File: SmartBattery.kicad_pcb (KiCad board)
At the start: 2 copper layers, 100 x 70 mm, 208 parts, among them J1 USB_C_Receptacle_USB2.0, J10 JST 2P-1.0, J11 JST 2P-1.0, J2 ST-USB-003A, J3 Barrel_Jack_MountingPin, J4 JST 2P-1.0, J5 JST 2P-1.0, J6 JST 2P-1.0, J7 JST 2P-1.0, J8 JST 2P-1.0, J9 JST 2P-1.0, Q1 AO4407A, Q10 AON7400A, Q11 AON7400A, Q12 AON7400A, Q13 AON7400A, Q2 2n7002K, Q3 AON7400A, Q4 AON7400A, Q5 AON7400A, Q6 AON7400A, Q7 2n7002K, Q8 AON7400A, Q9 AON7400A, SW1 SW_Push, SW2 SW_Push, U1 bq2477x, U10 ESP32-WROOM-32U, U2 BQ294706DSGR, U3 ITV4030, U4 BQ40Z50, U5 LM5175PWPR, U6 STM32F730R8T6, U7 W25Q128JVSIQ, U8 TPS54202HDDCR, U9 FS35ND01G-S1Y2QWFI000, Y1 Q13FC1350000400, Y2 Crystal_GND24

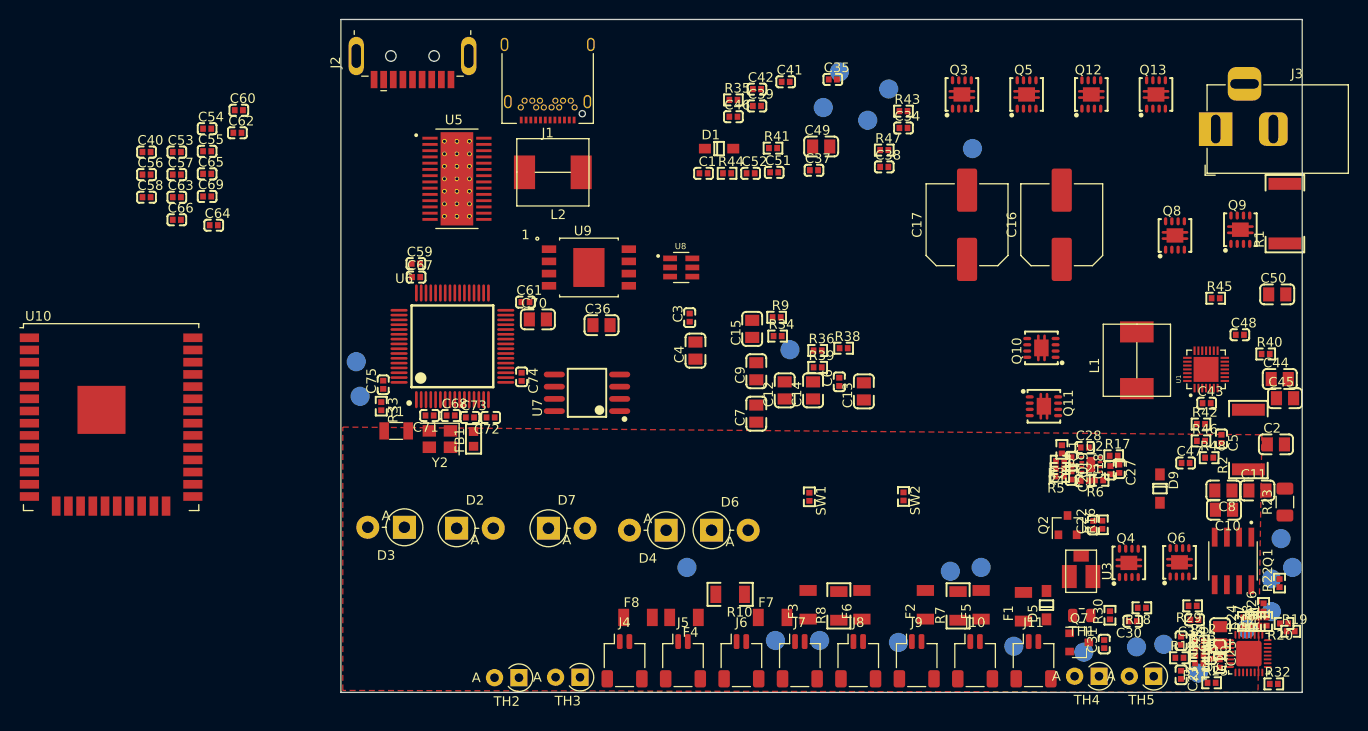
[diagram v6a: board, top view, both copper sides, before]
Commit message: Replaced old charger to support JLC assembly. Very close now!
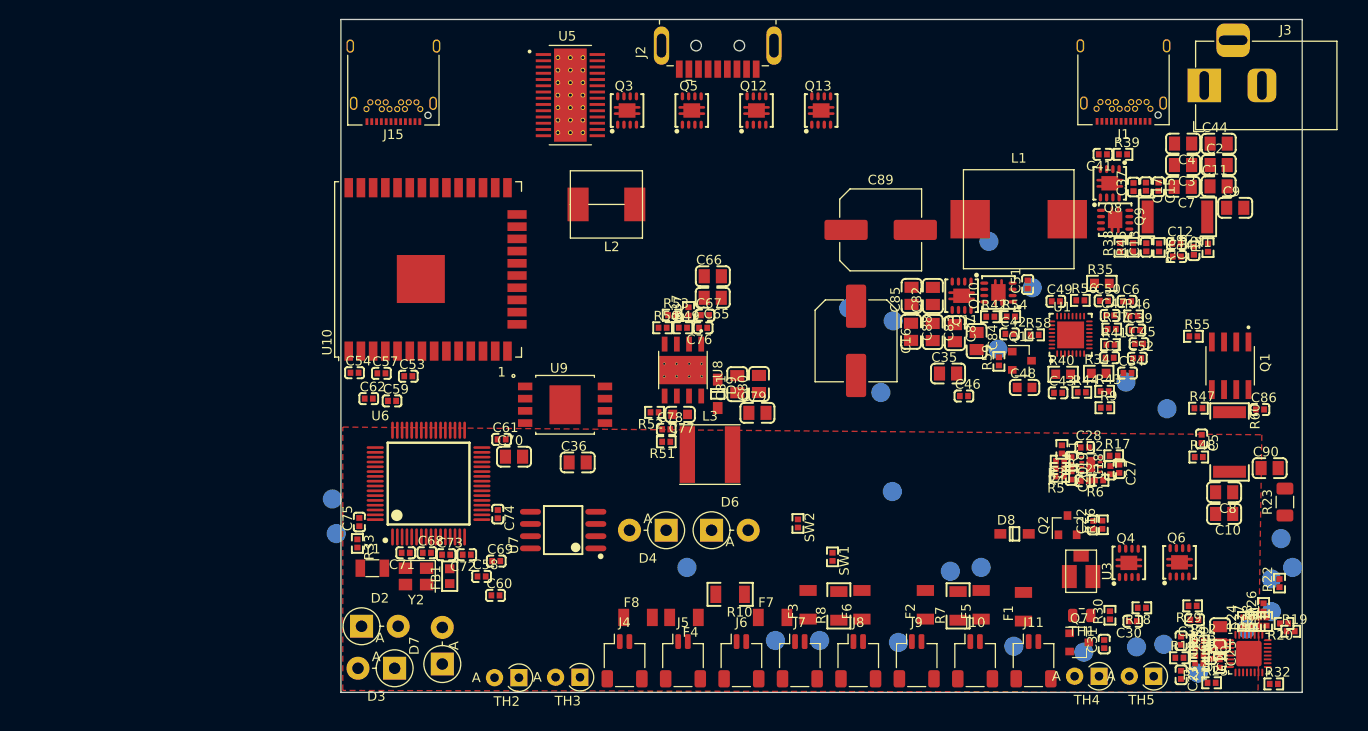
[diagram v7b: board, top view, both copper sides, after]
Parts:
- removed C40, C55, C56, C63, C64: 0.1u 6.3v, lc_lib:0402_C
- removed D1: CD1206-S01575, lc_lib:SOD-123
- removed D5: DIODE, lc_lib:SOD-123
- added C76: 0.1u 25v, lc_lib:0402_C, F.Cu at (37.7, 32.1)
- added C77: 8.2nF, lc_lib:0603_C, F.Cu at (35.3, 41.1)
- added C78: 220pF, lc_lib:0402_C, F.Cu at (33.8, 42.6)
- added C79: 22u, lc_lib:0805_C, F.Cu at (43.3, 40.9)
- added C80: 22u, lc_lib:0805_C, F.Cu at (43.5, 37.9)
- added C81: 22u, lc_lib:0805_C, F.Cu at (41.2, 37.9)
- added C82: 10u, lc_lib:0805_C, F.Cu at (61.6, 28.8)
- added C83: 10u, lc_lib:0805_C, F.Cu at (61.6, 32.5)
- added C84: 10u, lc_lib:0805_C, F.Cu at (66.1, 33.5)
- added C85: 10u, lc_lib:0805_C, F.Cu at (59.4, 28.8)
- added C86: 1uF 25v, lc_lib:0402_C, F.Cu at (95.6, 40.6)
- added C87: 22u, lc_lib:0805_C, F.Cu at (63.9, 32.6)
- added C88: 22u, lc_lib:0805_C, F.Cu at (59.3, 32.5)
- added C89: 220u, Capacitor_SMD:C_Elec_8x10.2, F.Cu at (56.1, 21.9)
- added C90: 22u, lc_lib:0805_C, F.Cu at (96.6, 46.7)
- added D8: B5817W-5819W, lc_lib:SOD-123, F.Cu at (70.1, 53.5)
- added J15: USB_C_Receptacle_USB2.0, Connector_USB:USB_C_Receptacle_Amphenol_12401548E4-2A, F.Cu at (5.46, 5.61)
- added L3: 6.8uH 47mO SWPA6028S6R8MT, Inductor_SMD:L_Taiyo-Yuden_NR-60xx, F.Cu at (38.4, 45.3)
- added Q14: 2n7002K, Package_TO_SOT_SMD:SOT-23, F.Cu at (70.8, 35.5)
- added R37: 0, lc_lib:0402_R, F.Cu at (36.2, 30.4)
- added R49: 0, lc_lib:0402_R, F.Cu at (35.6, 32.1)
- added R50: 20k, lc_lib:0402_R, F.Cu at (33.5, 32.1)
- added R51: 51k, lc_lib:0402_R, F.Cu at (33.8, 43.9)
- added R52: 15k, lc_lib:0402_R, F.Cu at (32.6, 40.9)
- added R53: DNP, lc_lib:0402_R, F.Cu at (34.5, 30.8)
- added R54: 0, lc_lib:0402_R, F.Cu at (69.7, 30.9)
- added R55: 0, lc_lib:0402_R, F.Cu at (88.7, 33.0)
- added R56: 110k, lc_lib:0402_R, F.Cu at (76.9, 29.2)
- added R57: DNP, lc_lib:0402_R, F.Cu at (80.2, 32.2)
- added R58: DNP, lc_lib:0402_R, F.Cu at (72.2, 32.8)
- added R59: 110k, lc_lib:0402_R, F.Cu at (68.5, 35.6)
- added R60: 0.01, lc_lib:2512_R, F.Cu at (92.4, 44.0)
- added TP25: TestPoint, TestPoint:TestPoint_Pad_D2.0mm, B.Cu at (71.9, 27.9)
- added TP26: TestPoint, TestPoint:TestPoint_Pad_D2.0mm, B.Cu at (67.4, 23.1)
- added TP27: TestPoint, TestPoint:TestPoint_Pad_D2.0mm, B.Cu at (85.9, 40.5)
- C1: value 1uF -> 0.1uF 6.3v
- C12: value 22u -> DNP; footprint lc_lib:0805_C -> lc_lib:0402_C
- C13: value 22u -> 1uF 25v; footprint lc_lib:0805_C -> lc_lib:0402_C
- C14, C15: value 22u -> 33nF; footprint lc_lib:0805_C -> lc_lib:0402_C
- C17: value 220u -> 33nF; footprint Capacitor_SMD:C_Elec_8x10.2 -> lc_lib:0402_C
- C3: value 0.1u 25v -> 10u; footprint lc_lib:0402_C -> lc_lib:0805_C
- C34: value 1uF 16v -> 0.1uF 6.3v
- C35: value 1uF 16v -> 2.2u 50v; footprint lc_lib:0402_C -> lc_lib:0805_C
- C37: value 1uF 25v -> 150pF
- C38: value 0.1uF 25v -> 33nF
- C39: value 0.1uF -> 33pF
- C4, C7, C9: value 22u -> 10u
- C41: value 0.1uF 25v -> 150pF
- C42: value 0.01uF -> 150pF
- C43: value 1uF 25v -> 0.1uF 25v
- C45: value 2.2uF 25v -> 150pF; footprint lc_lib:0805_C -> lc_lib:0402_C
- C46: value 2200pF -> 0.1uF 25v
- C47: value 0.1uF -> 1.5nF
- C48: value 1uF 25v -> 680pF; footprint lc_lib:0402_C -> lc_lib:0603_C
- C49: value 10u -> 15pF; footprint lc_lib:0805_C -> lc_lib:0402_C
- C50: value 10u -> 1uF 16v; footprint lc_lib:0805_C -> lc_lib:0402_C
- C51: value 47n -> 150pF
- C52: value 0.1uF 25v -> 1uF 16v
- C6: value 0.1u 25v -> 0.1uF 6.3v
- C65, C66: value 0.1u 6.3v -> 10u; footprint lc_lib:0402_C -> lc_lib:0805_C
- C67: value 0.1u 6.3v -> 0.1u 25v
- D9: value CD1206-S01575 -> B5817W-5819W
- L1: value MWSA0603-2R2MT -> MWSA1004-2R2MT; footprint SmartBattery:MWSA0603 -> SmartBattery:L_10.3x11.5_H4
- R2: value 0.01 -> 4.7; footprint lc_lib:2512_R -> lc_lib:0402_R
- R34: value 10M -> 27k; footprint lc_lib:0402_R -> lc_lib:0603_R
- R35: value DNP -> 110k; footprint lc_lib:0402_R -> lc_lib:0603_R
- R36: value 0 -> 4.7
- R39: value 1M -> 0
- R40: value 430k -> 40.2k; footprint lc_lib:0402_R -> lc_lib:0603_R
- R41: value 100k -> 10k
- R42: value 4.7 -> 0
- R43, R44: value 4.02k -> 0
- R45: value 10 -> 1
- R46, R47: value 0 -> 10
- R48: value 4.7 -> 10
- R9: value 10M -> 33k
- U1: value bq2477x -> BQ25703ARSNR; footprint SmartBattery:QFN40P400X400X80-29N -> lc_lib:VQFN-32_4X4X04P
- U8: value TPS54202HDDCR -> LMR14030SDDAR; footprint SmartBattery:SOT95P280X110-6N -> SmartBattery:NOPB
- moved J1 59.9 mm to (81.4, 5.58)
- moved C60 57.1 mm to (16.1, 59.9)
- moved C66 56.1 mm to (38.7, 26.7)
- moved C4 55.1 mm to (87.6, 12.9), turned to 180 degrees
- moved C65 54.2 mm to (38.7, 28.9), turned to 180 degrees
- moved C3 53.7 mm to (87.6, 15.1), turned to 180 degrees
- moved C58 52.6 mm to (14.6, 57.9)
- moved C9 52.6 mm to (93.0, 19.6), turned to 0 degrees
- moved C7 50.2 mm to (87.6, 17.4), turned to 180 degrees
- moved C69 48.4 mm to (16.2, 56.3)
- moved D9 47.0 mm to (39.2, 38.9)
- moved C1 46.4 mm to (80.0, 35.2)
- moved C39 45.8 mm to (82.7, 32.3)
- moved C15 44.8 mm to (85.0, 17.4), turned to 270 degrees
- moved C52 44.6 mm to (82.8, 35.2)
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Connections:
- net /Charger/ACOK renamed /Charger/EN_OTG
- net Net-(J2-Pad1) renamed /OutputStage/OUTPUT_VOLTAGE
- C10 pad 1: Net-(C10-Pad1) -> /Battery connection and protection/BATT_PACK_P
- C11 pad 1: Net-(C10-Pad1) -> /Charger/ADAPTER_IN
- C12 pad 1: /Charger/VSYS -> Net-(C12-Pad1)
- C12 pad 2: GND -> Net-(C12-Pad2)
- C13 pad 1: /Charger/VSYS -> GND
- C13 pad 2: GND -> Net-(C13-Pad2)
- C14 pad 1: /Charger/VSYS -> Net-(C12-Pad1)
- C15 pad 1: /Charger/VSYS -> GND
- C15 pad 2: GND -> Net-(C15-Pad2)
- C17 pad 1: /Charger/VSYS -> GND
- C17 pad 2: GND -> Net-(C15-Pad2)
- C2 pad 1: /Charger/VSYS -> /Charger/ADAPTER_IN
- C3 pad 1: /Charger/VSYS -> /Charger/ADAPTER_IN
- C36 pad 2: /MCU/Power_3p3v -> /Peripheral_3p3v/3p3v
- C37 pad 1: GND -> Net-(C15-Pad2)
- C37 pad 2: Net-(C37-Pad2) -> GND
- C38 pad 1: Net-(C37-Pad2) -> GND
- C38 pad 2: GND -> Net-(C12-Pad2)
- C39 pad 1: Net-(C37-Pad2) -> GND
- C4 pad 1: /Charger/VSYS -> /Charger/ADAPTER_IN
- C41 pad 1: Net-(C39-Pad2) -> GND
- C41 pad 2: GND -> Net-(C41-Pad2)
- C43 pad 1: GND -> Net-(C43-Pad1)
- C43 pad 2: /Charger/BQ_VCC -> Net-(C43-Pad2)
- C45 pad 1: /Charger/ADAPTER_IN -> GND
- C45 pad 2: GND -> Net-(C42-Pad2)
- C46 pad 2: /Charger/ADAPTER_IN -> Net-(C46-Pad2)
- C47 pad 1: Net-(C47-Pad1) -> GND
- C47 pad 2: Net-(C46-Pad1) -> Net-(C42-Pad2)
- C48 pad 1: GND -> Net-(C48-Pad1)
- C48 pad 2: Net-(C39-Pad2) -> GND
- C49 pad 1: Net-(C39-Pad2) -> Net-(C49-Pad1)
- C5 pad 1: /Charger/VSYS -> Net-(C5-Pad1)
- C5 pad 2: Net-(C10-Pad1) -> /Battery connection and protection/BATT_PACK_P
- C50 pad 1: Net-(C39-Pad2) -> Net-(C50-Pad1)
- C51 pad 1: Net-(C51-Pad1) -> GND
- C52 pad 1: /Battery connection and protection/BATT_PACK_P -> Net-(C52-Pad1)
- C53 pad 1: /MCU/Power_3p3v -> /Peripheral_3p3v/3p3v
- C54 pad 1: /MCU/Power_3p3v -> /Peripheral_3p3v/3p3v
- C57 pad 1: /MCU/Power_3p3v -> /Peripheral_3p3v/3p3v
- C59 pad 1: /MCU/Power_3p3v -> /Peripheral_3p3v/3p3v
- C6 pad 1: Net-(C10-Pad1) -> GND
- C6 pad 2: GND -> /Charger/PSYS
- C61 pad 1: /MCU/Power_3p3v -> /Peripheral_3p3v/3p3v
- C62 pad 1: /MCU/Power_3p3v -> /Peripheral_3p3v/3p3v
- C65 pad 1: /MCU/Power_3p3v -> GND
- C65 pad 2: GND -> /Peripheral_3p3v/VSYS_IN_3p3
- C66 pad 1: /MCU/Power_3p3v -> /Peripheral_3p3v/VSYS_IN_3p3
- C67 pad 1: /MCU/Power_3p3v -> /Peripheral_3p3v/VSYS_IN_3p3
- C7 pad 1: /Charger/VSYS -> /Charger/ADAPTER_IN
- C74 pad 1: /MCU/Power_3p3v -> /Peripheral_3p3v/3p3v
- C75 pad 1: /MCU/Power_3p3v -> /Peripheral_3p3v/3p3v
- C8 pad 1: Net-(C10-Pad1) -> /Battery connection and protection/BATT_PACK_P
- C9 pad 1: /Charger/VSYS -> /Charger/ADAPTER_IN
- D9 pad 1: /Charger/BQ_VCC -> Net-(D9-Pad1)
- D9 pad 2: /Battery connection and protection/BATT_PACK_P -> GND
- FB1 pad 1: /MCU/Power_3p3v -> /Peripheral_3p3v/3p3v
- J2 pad 4: Net-(J2-Pad4) -> GND
- J2 pad 5: Net-(J2-Pad5) -> GND
- J3 pad 1: Net-(J3-Pad1) -> /Charger/ADAPTER_IN
- J3 pad 2: Net-(J3-Pad2) -> GND
- L1 pad 1: /Charger/VSYS -> Net-(C46-Pad1)
- L1 pad 2: Net-(C51-Pad1) -> Net-(C43-Pad1)
- Q1 pad 1: Net-(C10-Pad1) -> /Charger/VSYS
- Q1 pad 2: Net-(C10-Pad1) -> /Charger/VSYS
- Q1 pad 3: Net-(C10-Pad1) -> /Charger/VSYS
- Q1 pad 5: /Battery connection and protection/BATT_PACK_P -> Net-(C5-Pad1)
- Q1 pad 6: /Battery connection and protection/BATT_PACK_P -> Net-(C5-Pad1)
- Q1 pad 7: /Battery connection and protection/BATT_PACK_P -> Net-(C5-Pad1)
- Q1 pad 8: /Battery connection and protection/BATT_PACK_P -> Net-(C5-Pad1)
- Q10 pad 1: Net-(C51-Pad1) -> GND
- Q10 pad 2: Net-(C51-Pad1) -> GND
- Q10 pad 3: Net-(C51-Pad1) -> GND
- Q10 pad 4: Net-(Q10-Pad4) -> Net-(C51-Pad2)
- Q10 pad 5: Net-(C39-Pad2) -> Net-(C46-Pad1)
- Q10 pad 6: Net-(C39-Pad2) -> Net-(C46-Pad1)
- Q10 pad 7: Net-(C39-Pad2) -> Net-(C46-Pad1)
- Q10 pad 8: Net-(C39-Pad2) -> Net-(C46-Pad1)
- Q11 pad 1: GND -> Net-(C46-Pad1)
- Q11 pad 2: GND -> Net-(C46-Pad1)
- Q11 pad 3: GND -> Net-(C46-Pad1)
- Q11 pad 5: Net-(C51-Pad1) -> /Charger/VSYS
- Q11 pad 6: Net-(C51-Pad1) -> /Charger/VSYS
- Q11 pad 7: Net-(C51-Pad1) -> /Charger/VSYS
- Q11 pad 8: Net-(C51-Pad1) -> /Charger/VSYS
- Q8 pad 1: Net-(C47-Pad1) -> GND
- Q8 pad 2: Net-(C47-Pad1) -> GND
- Q8 pad 3: Net-(C47-Pad1) -> GND
- Q8 pad 4: Net-(Q8-Pad4) -> Net-(C41-Pad2)
- Q8 pad 5: /Charger/ADAPTER_IN -> Net-(C43-Pad1)
- Q8 pad 6: /Charger/ADAPTER_IN -> Net-(C43-Pad1)
- Q8 pad 7: /Charger/ADAPTER_IN -> Net-(C43-Pad1)
- Q8 pad 8: /Charger/ADAPTER_IN -> Net-(C43-Pad1)
- Q9 pad 1: Net-(C47-Pad1) -> Net-(C43-Pad1)
- Q9 pad 2: Net-(C47-Pad1) -> Net-(C43-Pad1)
- Q9 pad 3: Net-(C47-Pad1) -> Net-(C43-Pad1)
- Q9 pad 4: Net-(Q8-Pad4) -> Net-(Q9-Pad4)
- Q9 pad 5: Net-(C37-Pad2) -> Net-(C15-Pad2)
- Q9 pad 6: Net-(C37-Pad2) -> Net-(C15-Pad2)
- Q9 pad 7: Net-(C37-Pad2) -> Net-(C15-Pad2)
- Q9 pad 8: Net-(C37-Pad2) -> Net-(C15-Pad2)
- R1 pad 1: Net-(C39-Pad2) -> /Charger/ADAPTER_IN
- R1 pad 2: Net-(C37-Pad2) -> Net-(C15-Pad2)
- R2 pad 1: Net-(C10-Pad1) -> Net-(C15-Pad2)
- R2 pad 2: /Charger/VSYS -> Net-(C12-Pad1)
- R33 pad 1: /MCU/Power_3p3v -> /Peripheral_3p3v/3p3v
- R34 pad 1: /Charger/REGN -> GND
- R35 pad 1: Net-(C42-Pad2) -> /Charger/IADP
- R35 pad 2: /Charger/REGN -> Net-(R34-Pad2)
- R36 pad 1: Net-(R36-Pad1) -> /Charger/ADAPTER_IN
- R36 pad 2: Net-(C37-Pad2) -> Net-(C12-Pad2)
- R38 pad 1: Net-(R38-Pad1) -> Net-(Q9-Pad4)
- R38 pad 2: Net-(C39-Pad2) -> Net-(R38-Pad2)
- R39 pad 1: Net-(C42-Pad2) -> Net-(R39-Pad1)
- R39 pad 2: GND -> Net-(C41-Pad2)
- R40 pad 1: Net-(R40-Pad1) -> Net-(C39-Pad2)
- R40 pad 2: /Charger/ADAPTER_IN -> Net-(C42-Pad2)
- R41 pad 1: GND -> Net-(C49-Pad1)
- R41 pad 2: Net-(R40-Pad1) -> Net-(C48-Pad1)
- R42 pad 1: Net-(Q8-Pad4) -> Net-(R42-Pad1)
- R42 pad 2: Net-(C46-Pad1) -> Net-(C51-Pad2)
- R43 pad 1: Net-(C47-Pad1) -> Net-(R43-Pad1)
- R44 pad 1: Net-(C46-Pad1) -> Net-(R44-Pad1)
- R45 pad 1: Net-(R45-Pad1) -> Net-(C13-Pad2)
- R45 pad 2: /Charger/BQ_VCC -> Net-(C15-Pad2)
- R46 pad 1: Net-(R46-Pad1) -> /Charger/REGN
- R46 pad 2: Net-(Q10-Pad4) -> Net-(C50-Pad1)
- R47 pad 2: Net-(Q11-Pad4) -> Net-(C5-Pad1)
- R48 pad 1: /Battery connection and protection/BATT_PACK_P -> Net-(R48-Pad1)
- R48 pad 2: Net-(R48-Pad2) -> /Battery connection and protection/BATT_PACK_P
- R9 pad 2: /Charger/PMON -> /Charger/PSYS
- TP20 pad 1: Net-(C47-Pad1) -> Net-(C43-Pad1)
- TP21 pad 1: Net-(C37-Pad2) -> Net-(C12-Pad1)
- TP22 pad 1: Net-(C39-Pad2) -> Net-(C12-Pad2)
- U1 pad 1: Net-(R38-Pad1) -> Net-(C13-Pad2)
- U1 pad 10: /Charger/PROCHOT_N -> /Charger/PSYS
- U1 pad 11: /Charger/CHARGER_SDA -> /Charger/PROCHOT_N
- U1 pad 12: /Charger/CHARGER_SCL -> /Charger/CHARGER_SDA
- U1 pad 13: Net-(U1-Pad13) -> /Charger/CHARGER_SCL
- U1 pad 14: Net-(U1-Pad14) -> Net-(R43-Pad2)
- U1 pad 15: Net-(U1-Pad15) -> Net-(R44-Pad1)
- U1 pad 16: Net-(R34-Pad2) -> Net-(C39-Pad2)
- U1 pad 17: Net-(R48-Pad2) -> Net-(C49-Pad1)
- U1 pad 18: Net-(Q1-Pad4) -> Net-(Q14-Pad2)
- U1 pad 19: /Charger/VSYS -> Net-(R48-Pad1)
- U1 pad 2: Net-(R36-Pad1) -> Net-(C12-Pad1)
- U1 pad 20: Net-(C10-Pad1) -> Net-(R47-Pad1)
- U1 pad 21: Net-(C42-Pad2) -> Net-(R55-Pad1)
- U1 pad 22: GND -> /Charger/VSYS
- U1 pad 23: Net-(R47-Pad1) -> Net-(C46-Pad1)
- U1 pad 24: /Charger/REGN -> Net-(R54-Pad1)
- U1 pad 25: (no net) -> Net-(C46-Pad2)
- U1 pad 26: Net-(R46-Pad1) -> Net-(R42-Pad1)
- U1 pad 27: Net-(C51-Pad1) -> GND
- U1 pad 28: Net-(R45-Pad1) -> /Charger/REGN
- U1 pad 29: GND -> Net-(R39-Pad1)
- U1 pad 3: Net-(R43-Pad2) -> Net-(C12-Pad2)
- U1 pad 4: Net-(R44-Pad2) -> /Charger/CHRG_OK
- U1 pad 6: Net-(R40-Pad1) -> Net-(C52-Pad1)
- U1 pad 7: /Charger/IADP -> Net-(C50-Pad1)
- U1 pad 8: /Charger/IBAT -> /Charger/IADP
- U1 pad 9: /Charger/PMON -> /Charger/IBAT
- U6 pad 19: /MCU/Power_3p3v -> /Peripheral_3p3v/3p3v
- U6 pad 32: /MCU/Power_3p3v -> /Peripheral_3p3v/3p3v
- U6 pad 48: /MCU/Power_3p3v -> /Peripheral_3p3v/3p3v
- U6 pad 64: /MCU/Power_3p3v -> /Peripheral_3p3v/3p3v
- U7 pad 8: /MCU/Power_3p3v -> /Peripheral_3p3v/3p3v
- U8 pad 2: Net-(U8-Pad2) -> /Peripheral_3p3v/VSYS_IN_3p3
- U9 pad 8: /MCU/Power_3p3v -> /Peripheral_3p3v/3p3v
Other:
- copper layers 2 -> 4
- net class Default: clearance 0.18 -> 0.13; trace_width 0.18 -> 0.13; via_dia 0.4 -> 0.45; via_drill 0.3 -> 0.25
- rule trace_clearance: 0.18 -> 0.13
- rule trace_min: 0.16 -> 0.12
- rule via_min_drill: 0.3 -> 0.25
- rule via_min_size: 0.4 -> 0.45

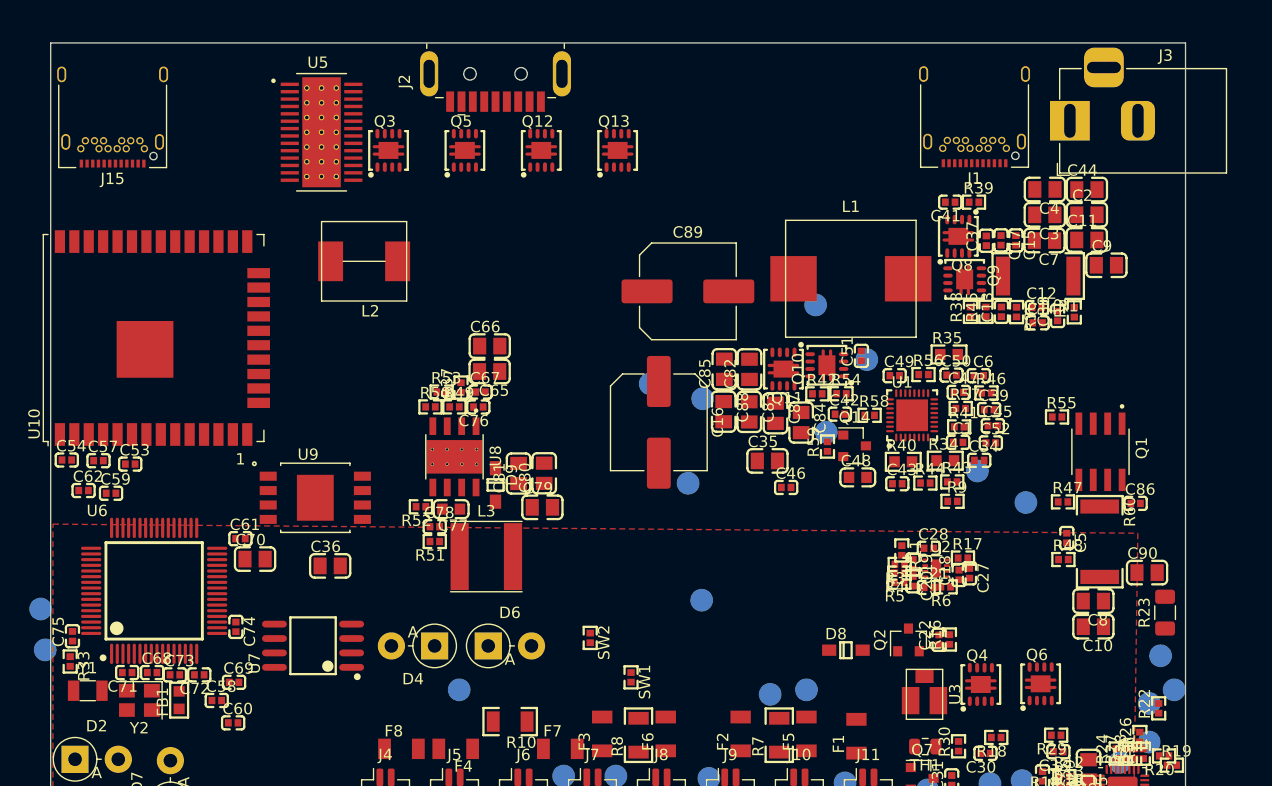
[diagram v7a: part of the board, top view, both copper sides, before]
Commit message: Both type-c ports are done! Only outputstage left.
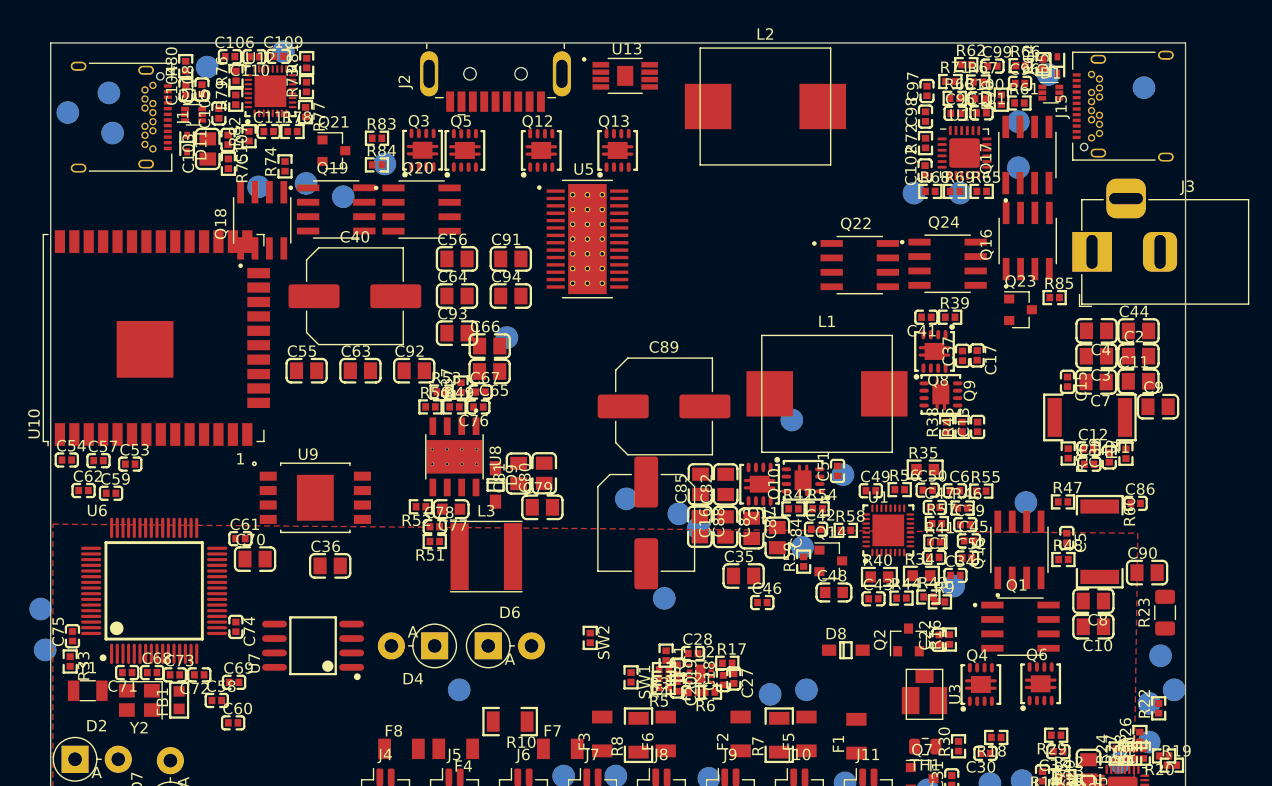
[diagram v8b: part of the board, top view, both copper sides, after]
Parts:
- added C100: 1uF 25v, lc_lib:0402_C, F.Cu at (81.9, 4.92)
- added C101: 1uF 25v, lc_lib:0402_C, F.Cu at (82.0, 6.16)
- added C102: 1uF 25v, lc_lib:0402_C, F.Cu at (77.0, 11.2)
- added C103: 10u, lc_lib:0805_C, F.Cu at (13.8, 9.34)
- added C104: 150pF, lc_lib:0402_C, F.Cu at (11.9, 4.16)
- added C105: 150pF, lc_lib:0402_C, F.Cu at (14.8, 6.21)
- added C106: 1uF 25v, lc_lib:0402_C, F.Cu at (15.8, 1.21)
- added C107: 1uF 25v, lc_lib:0402_C, F.Cu at (15.6, 8.54)
- added C108: 1uF 25v, lc_lib:0402_C, F.Cu at (13.3, 4.11)
- added C109: 1uF 25v, lc_lib:0402_C, F.Cu at (20.1, 1.18)
- added C110: 1uF 25v, lc_lib:0402_C, F.Cu at (17.9, 1.22)
- added C111: 1uF 25v, lc_lib:0402_C, F.Cu at (19.2, 7.80)
- added C40: 220u, Capacitor_SMD:C_Elec_8x10.2, F.Cu at (26.8, 22.3)
- added C55: 22u, lc_lib:0805_C, F.Cu at (22.6, 28.9)
- added C56: 22u, lc_lib:0805_C, F.Cu at (35.8, 19.0)
- added C63: 22u, lc_lib:0805_C, F.Cu at (27.3, 28.9)
- added C64: 22u, lc_lib:0805_C, F.Cu at (35.8, 22.3)
- added C91: 22u, lc_lib:0805_C, F.Cu at (40.5, 19.0)
- added C92: 22u, lc_lib:0805_C, F.Cu at (32.0, 28.9)
- added C93: 22u, lc_lib:0805_C, F.Cu at (35.8, 25.6)
- added C94: 22u, lc_lib:0805_C, F.Cu at (40.5, 22.3)
- added C95: 150pF, lc_lib:0402_C, F.Cu at (79.7, 6.20)
- added C96: 150pF, lc_lib:0402_C, F.Cu at (85.4, 3.56)
- added C97: 1uF 25v, lc_lib:0402_C, F.Cu at (77.2, 4.24)
- added C98: 1uF 25v, lc_lib:0402_C, F.Cu at (77.1, 6.49)
- added C99: 1uF 25v, lc_lib:0402_C, F.Cu at (83.0, 2.04)
- added D1: ESDA6V8AV6, Package_TO_SOT_SMD:SOT-563, F.Cu at (88.1, 4.38)
- added D10: ESDA6V8AV6, Package_TO_SOT_SMD:SOT-563, F.Cu at (12.6, 6.33)
- added D11: PESD24VS1UB-N, lc_lib:SOD-523, F.Cu at (12.0, 8.87)
- added D5: PESD24VS1UB-N, lc_lib:SOD-523, F.Cu at (88.7, 1.95)
- added Q15: VBA2625, SmartBattery:SOIC127P600X175-8N, F.Cu at (85.4, 44.7)
- added Q16: VBA2625, SmartBattery:SOIC127P600X175-8N, F.Cu at (86.1, 17.5)
- added Q17: VBA2625, SmartBattery:SOIC127P600X175-8N, F.Cu at (86.1, 9.88)
- added Q18: VBA2625, SmartBattery:SOIC127P600X175-8N, F.Cu at (18.6, 15.6)
- added Q19: VBA2625, SmartBattery:SOIC127P600X175-8N, F.Cu at (25.2, 14.7)
- added Q20: VBA2625, SmartBattery:SOIC127P600X175-8N, F.Cu at (32.7, 14.7)
- added Q21: 2n7002K, Package_TO_SOT_SMD:SOT-23, F.Cu at (25.0, 9.50)
- added Q22: VBA2625, SmartBattery:SOIC127P600X175-8N, F.Cu at (71.3, 19.6)
- added Q23: 2n7002K, Package_TO_SOT_SMD:SOT-23, F.Cu at (85.5, 23.5)
- added Q24: VBA2625, SmartBattery:SOIC127P600X175-8N, F.Cu at (79.0, 19.5)
- added R61: ??, lc_lib:0402_R, F.Cu at (85.4, 5.29)
- added R62: 100k, lc_lib:0402_R, F.Cu at (80.7, 1.91)
- added R63: 100k, lc_lib:0402_R, F.Cu at (79.7, 4.88)
- added R64: 0, lc_lib:0402_R, F.Cu at (87.4, 1.87)
- added R65: 100k, lc_lib:0402_R, F.Cu at (82.0, 13.1)
- added R66: 5.1k, lc_lib:0402_R, F.Cu at (85.5, 2.00)
- added R67: 5.1k, lc_lib:0402_R, F.Cu at (81.7, 3.44)
- added R68: 5.1k, lc_lib:0402_R, F.Cu at (77.5, 13.1)
- added R69: 100k, lc_lib:0402_R, F.Cu at (79.7, 13.1)
- added R70: 5.1k, lc_lib:0402_R, F.Cu at (83.8, 5.00)
- added R71: 5.1k, lc_lib:0402_R, F.Cu at (79.3, 3.40)
- added R72: 100k, lc_lib:0402_R, F.Cu at (77.1, 8.82)
- added R73: 100k, lc_lib:0402_R, F.Cu at (22.5, 3.89)
- added R74: ??, lc_lib:0402_R, F.Cu at (20.6, 10.9)
- added R75: 100k, lc_lib:0402_R, F.Cu at (15.7, 10.6)
- added R76: 100k, lc_lib:0402_R, F.Cu at (16.3, 2.91)
- added R77: 0, lc_lib:0402_R, F.Cu at (22.5, 6.09)
- added R78: 5.1k, lc_lib:0402_R, F.Cu at (21.3, 7.80)
- added R79: 5.1k, lc_lib:0402_R, F.Cu at (16.3, 5.00)
- added R80: 5.1k, lc_lib:0402_R, F.Cu at (11.9, 2.04)
- added R81: 100k, lc_lib:0402_R, F.Cu at (22.6, 1.77)
- added R82: 5.1k, lc_lib:0402_R, F.Cu at (17.5, 8.21)
- added R83: 100k, lc_lib:0402_R, F.Cu at (28.8, 8.40)
- added R84: 100k, lc_lib:0402_R, F.Cu at (28.8, 10.7)
- added R85: 100k, lc_lib:0402_R, F.Cu at (88.5, 22.4)
- added TP28: TestPoint, TestPoint:TestPoint_Pad_D2.0mm, B.Cu at (40.2, 26.0)
- added TP29: TestPoint, TestPoint:TestPoint_Pad_D2.0mm, B.Cu at (85.3, 11.0)
- added TP30: TestPoint, TestPoint:TestPoint_Pad_D2.0mm, B.Cu at (76.1, 13.2)
- added TP31: TestPoint, TestPoint:TestPoint_Pad_D2.0mm, B.Cu at (96.3, 3.94)
- added TP32: TestPoint, TestPoint:TestPoint_Pad_D2.0mm, B.Cu at (87.9, 2.79)
- added TP33: TestPoint, TestPoint:TestPoint_Pad_D2.0mm, B.Cu at (85.3, 6.94)
- added TP34: TestPoint, TestPoint:TestPoint_Pad_D2.0mm, B.Cu at (80.1, 13.2)
- added TP35: TestPoint, TestPoint:TestPoint_Pad_D2.0mm, B.Cu at (5.46, 7.94)
- added TP36: TestPoint, TestPoint:TestPoint_Pad_D2.0mm, B.Cu at (1.51, 6.13)
- added TP37: TestPoint, TestPoint:TestPoint_Pad_D2.0mm, B.Cu at (5.13, 4.40)
- added TP38: TestPoint, TestPoint:TestPoint_Pad_D2.0mm, B.Cu at (20.5, 0.77)
- added TP39: TestPoint, TestPoint:TestPoint_Pad_D2.0mm, B.Cu at (13.8, 2.13)
- added TP40: TestPoint, TestPoint:TestPoint_Pad_D2.0mm, B.Cu at (25.8, 13.6)
- added TP41: TestPoint, TestPoint:TestPoint_Pad_D2.0mm, B.Cu at (18.3, 12.7)
- added TP42: TestPoint, TestPoint:TestPoint_Pad_D2.0mm, B.Cu at (29.4, 10.7)
- added TP43: TestPoint, TestPoint:TestPoint_Pad_D2.0mm, B.Cu at (22.5, 12.4)
- added U11: STUSB4500, Package_DFN_QFN:QFN-24-1EP_4x4mm_P0.5mm_EP2.7x2.6mm, F.Cu at (80.5, 9.70)
- added U12: STUSB4700, lc_lib:VQFN-32_4X4X04P, F.Cu at (19.4, 4.25)
- added U13: TPS2511DGNR, SmartBattery:SOP65P490X110-9N, F.Cu at (50.6, 2.90)
- L2: footprint SmartBattery:MWSA0603 -> SmartBattery:L_10.3x11.5_H4
- Q1: value AO4407A -> VBA2625
- moved J15 90.0 mm to (95.4, 5.57), turned to 90 degrees
- moved J1 76.1 mm to (5.30, 6.54), turned to 270 degrees
- moved L2 39.0 mm to (63.0, 5.60)
- moved U5 25.2 mm to (47.3, 17.3)
- moved R4 22.7 mm to (54.0, 56.0)
- moved C19 22.7 mm to (55.2, 55.2)
- moved C20 22.7 mm to (55.2, 56.7)
- moved C28 22.7 mm to (56.6, 53.8)
- moved R11 22.7 mm to (54.2, 54.0)
- moved R17 22.7 mm to (59.6, 54.7)
- moved R3 22.7 mm to (54.0, 55.2)
- moved R6 22.7 mm to (58.1, 57.2)
- moved U2 22.7 mm to (57.2, 55.6)
- moved C18 22.7 mm to (59.3, 56.1)
- moved C21 22.7 mm to (56.6, 57.3)
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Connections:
- net /OutputStage/OUTPUT_VOLTAGE renamed Net-(J2-Pad1)
- J1 pad A1: Net-(J1-PadA1) -> GND
- J1 pad A12: Net-(J1-PadA1) -> GND
- J1 pad A6: Net-(J1-PadA6) -> /Type_C_Output/OUTPUT_DP
- J1 pad A7: Net-(J1-PadA7) -> /Type_C_Output/OUTPUT_DM
- J1 pad B1: Net-(J1-PadA1) -> GND
- J1 pad B12: Net-(J1-PadA1) -> GND
- J1 pad B6: Net-(J1-PadB6) -> /Type_C_Output/OUTPUT_DP
- J1 pad B7: Net-(J1-PadB7) -> /Type_C_Output/OUTPUT_DM
- J1 pad S1: Net-(J1-PadS1) -> GND
- J15 pad A1: Net-(J15-PadA1) -> GND
- J15 pad A12: Net-(J15-PadA1) -> GND
- J15 pad A6: Net-(J15-PadA6) -> /type_c_input/INPUT_DP
- J15 pad A7: Net-(J15-PadA7) -> /type_c_input/INPUT_DM
- J15 pad B1: Net-(J15-PadA1) -> GND
- J15 pad B12: Net-(J15-PadA1) -> GND
- J15 pad B6: Net-(J15-PadB6) -> /type_c_input/INPUT_DP
- J15 pad B7: Net-(J15-PadB7) -> /type_c_input/INPUT_DM
- J15 pad S1: Net-(J15-PadS1) -> GND
- J2 pad 4: GND -> Net-(J2-Pad4)
- J2 pad 5: GND -> Net-(J2-Pad5)
